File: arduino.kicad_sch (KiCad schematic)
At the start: 14 parts, among them J1 Conn_01x01_Female, J2 Conn_01x01_Female, J3 Conn_01x01_Female, J4 Conn_01x01_Female, J5 Conn_01x01_Female, J6 Conn_01x01_Female, J7 Conn_01x01_Female, U5 CD74HC4067SM, U6 LM358

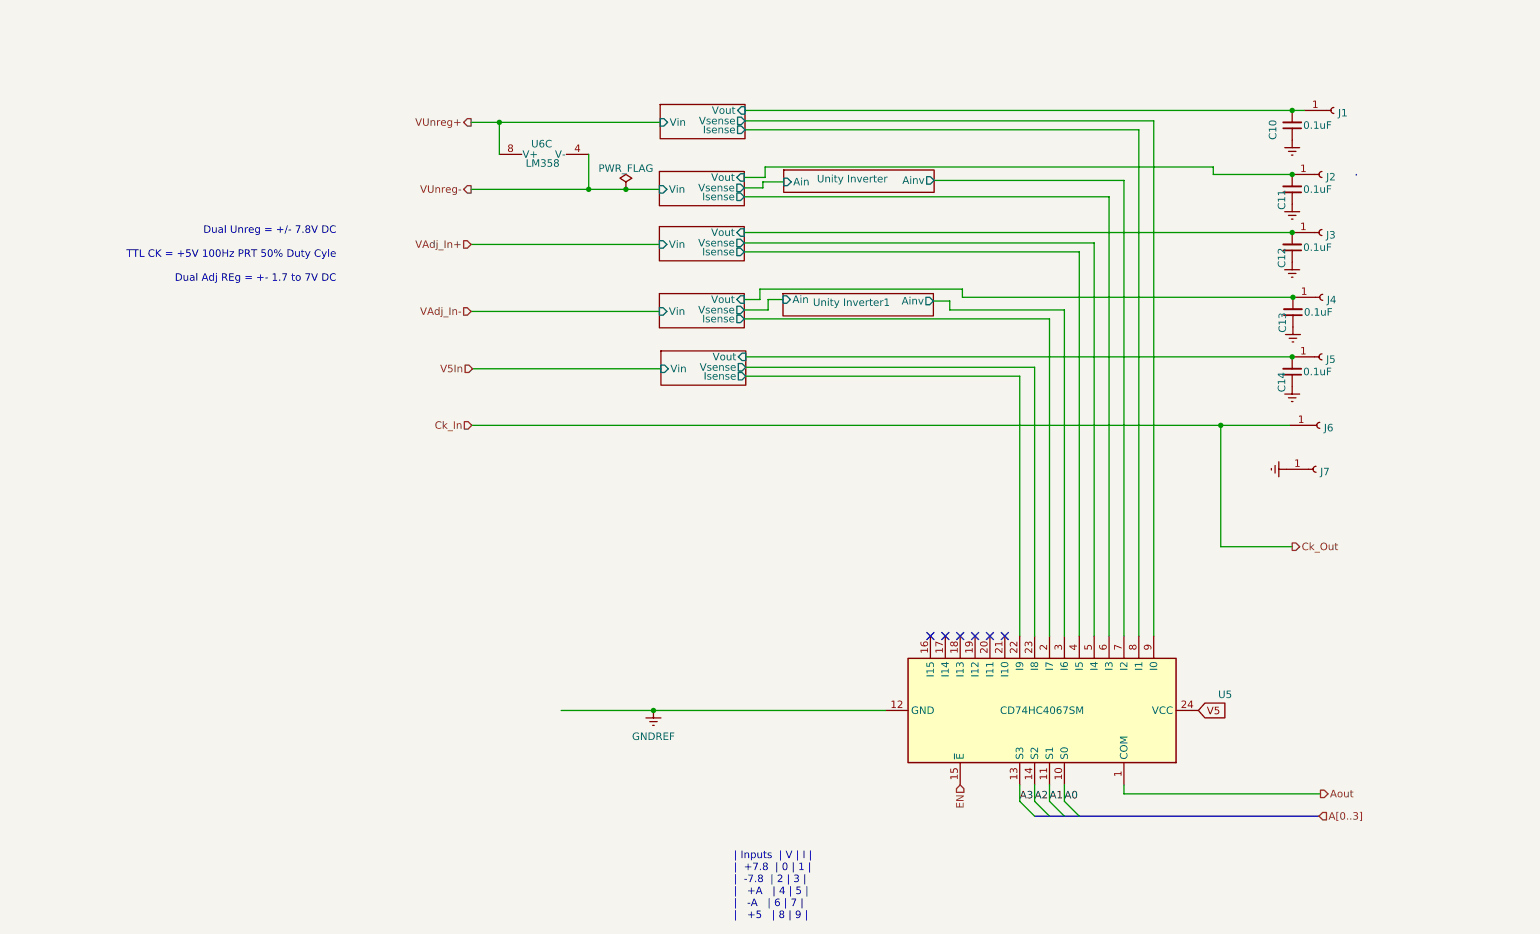
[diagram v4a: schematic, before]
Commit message: Updated improved board for all SMD
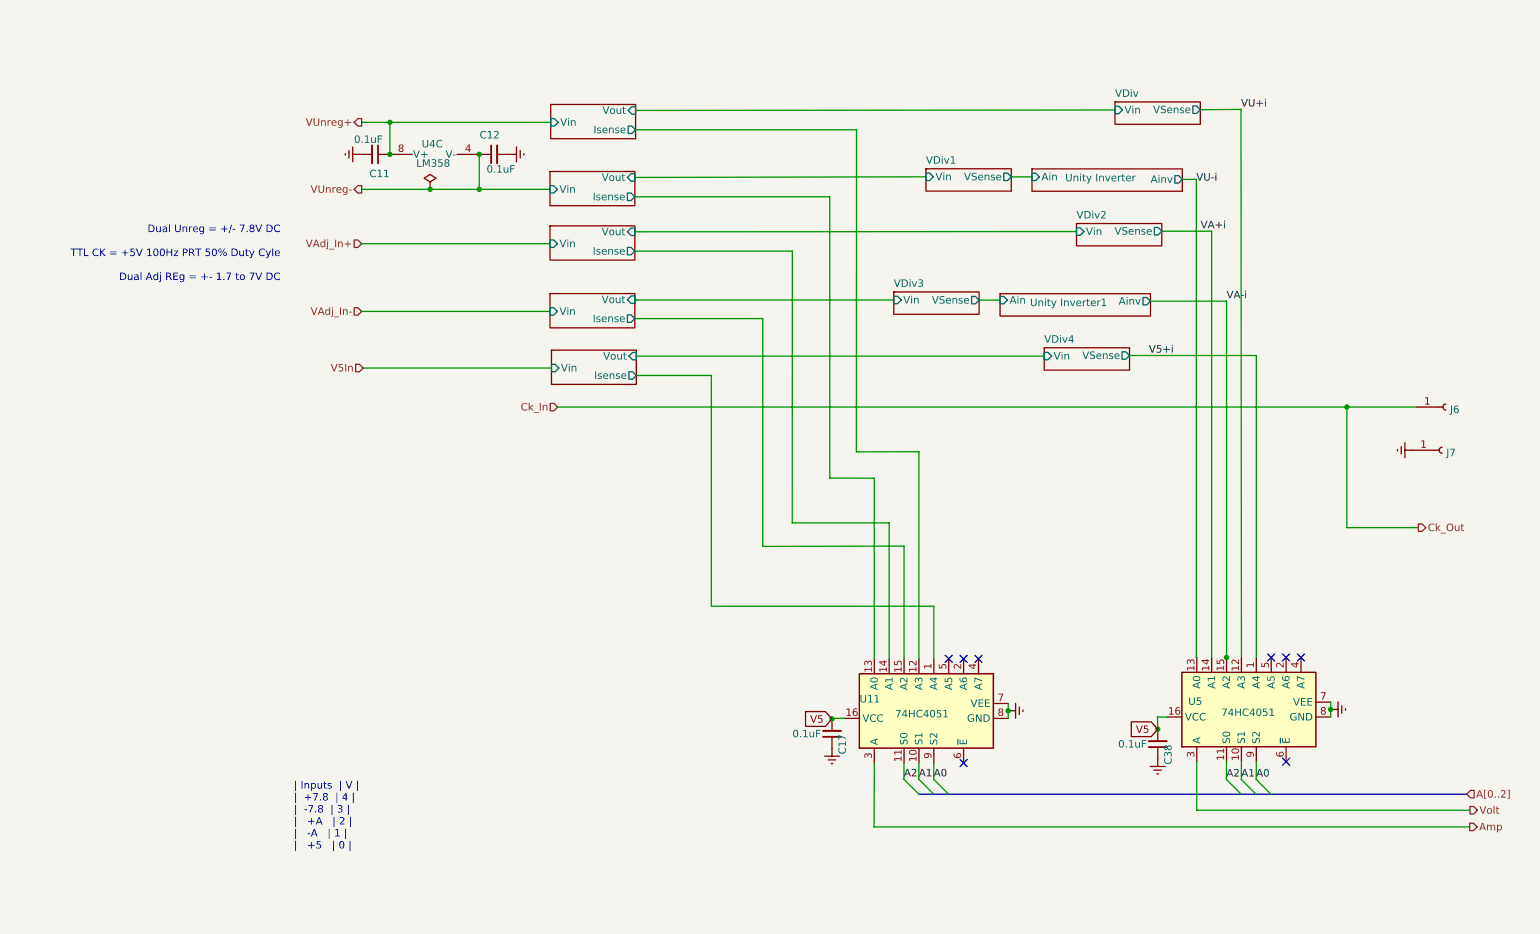
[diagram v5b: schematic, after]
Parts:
- removed C10, C13, C14: 0.1uF, Capacitor_SMD:C_0603_1608Metric, symbol Device:C_Small
- removed J1, J2, J3, J4, J5: Conn_01x01_Female, Connector_PinHeader_2.54mm:PinHeader_1x01_P2.54mm_Vertical, symbol Connector:Conn_01x01_Female
- removed U5: CD74HC4067SM, Package_SO:SSOP-24_5.3x8.2mm_P0.65mm, symbol 74xx:CD74HC4067SM
- added C17, C38: 0.1uF, Capacitor_SMD:C_0603_1608Metric, symbol Device:C_Small
- added U11, U5: 74HC4051, Package_SO:TSSOP-16-1EP_4.4x5mm_P0.65mm, symbol 74xx:74HC4051
- renumbered U6 to U4
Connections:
- net A0: now also U11.9 (S2), U5.9 (S2)
- net A1: now also U11.10 (S1), U5.10 (S1)
- net A2: now also U11.11 (S0), U5.11 (S0)
- net Curent and Volt4/Isense: now also U11.12 (A3)
- net Curent and Volt5/Isense: now also U11.13 (A0)
- net Curent and Volt5/Vout: no longer C11.2
- net Curent and Volt6/Isense: now also U11.14 (A1)
- net Curent and Volt6/Vout: no longer C12.2
- net Curent and Volt7/Isense: now also U11.15 (A2)
- net Curent and Volt8/Isense: now also U11.1 (A4)
- net GNDREF: now also C11.2, C12.2, C17.1, C38.1, U11.7 (VEE), U11.8 (GND), U5.7 (VEE), U5.8 (GND); no longer C11.1, C12.1
- net V5: now also C17.2, C38.2, U11.16 (VCC), U5.16 (VCC)
- net VUnreg+: now also C11.1
- net VUnreg-: now also C12.1
- new net Amp: U11.3 (A)
- new net V5+i: U5.1 (A4)
- new net VA+i: U5.14 (A1)
- new net VA-i: U5.15 (A2)
- new net VU+i: U5.12 (A3)
- new net VU-i: U5.13 (A0)
- new net Volt: U5.3 (A)
- no-connect marks 6 -> 8
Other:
- added sheet VDiv (VoltDivider.kicad_sch)
- added sheet VDiv1 (VoltDivider.kicad_sch)
- added sheet VDiv2 (VoltDivider.kicad_sch)
- added sheet VDiv3 (VoltDivider.kicad_sch)
- added sheet VDiv4 (VoltDivider.kicad_sch)
- sheet Curent and Volt4 ports: added none; removed Vsense
- sheet Curent and Volt5 ports: added none; removed Vsense
- sheet Curent and Volt6 ports: added none; removed Vsense
- sheet Curent and Volt7 ports: added none; removed Vsense
- sheet Curent and Volt8 ports: added none; removed Vsense
- note added: "| Inputs | V | | +7.8 | 4 | | -7.8 | 3 | | +A | 2 | | -A | 1 | | +5 | 0 |"
- note removed: "| Inputs | V | I | | +7.8 | 0 | 1 | | -7.8 | 2 | 3 | | +A | 4 | 5 | | -A | 6 | 7 | | +5 | 8 | 9 |"
- moved on the sheet: J6, J7, U4C

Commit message: added PDF schematic and images of board to date
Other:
- note removed: "| Inputs | V | | +7.8 | 4 | | -7.8 | 3 | | +A | 2 | | -A | 1 | | +5 | 0 |"
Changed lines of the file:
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@@
   (junction (at 89.789 41.656) (diameter 0) (color 0 0 0 0)
-  )
-  (junction (at 217.2716 127.4826) (diameter 0) (color 0 0 0 0)
   )
   (junction (at 237.7948 84.7598) (diameter 0) (color 0 0 0 0)
@@
     (stroke (width 0) (type default) (color 0 0 0 0))
   )
-  (wire (pts (xy 217.2716 127.7366) (xy 217.2716 127.4826))
-    (stroke (width 0) (type default) (color 0 0 0 0))
-  )
   (wire (pts (xy 149.5806 48.895) (xy 116.332 48.895))
     (stroke (width 0) (type default) (color 0 0 0 0))
@@
     (stroke (width 0) (type default) (color 0 0 0 0))
   )
-  (text "| Inputs  | V |\n|  +7.8  | 4 |\n|  -7.8  | 3 |\n|   +A   | 2 |\n|   -A   | 1 |\n|   +5   | 0 |"
-    (at 58.166 160.4772 0)
-    (effects (font (size 1.27 1.27)) (justify left bottom))
-  )
   (text "Dual Unreg = +/- 7.8V DC\n\nTTL CK = +5V 100Hz PRT 50% Duty Cyle\n\nDual Adj REg = +- 1.7 to 7V DC"

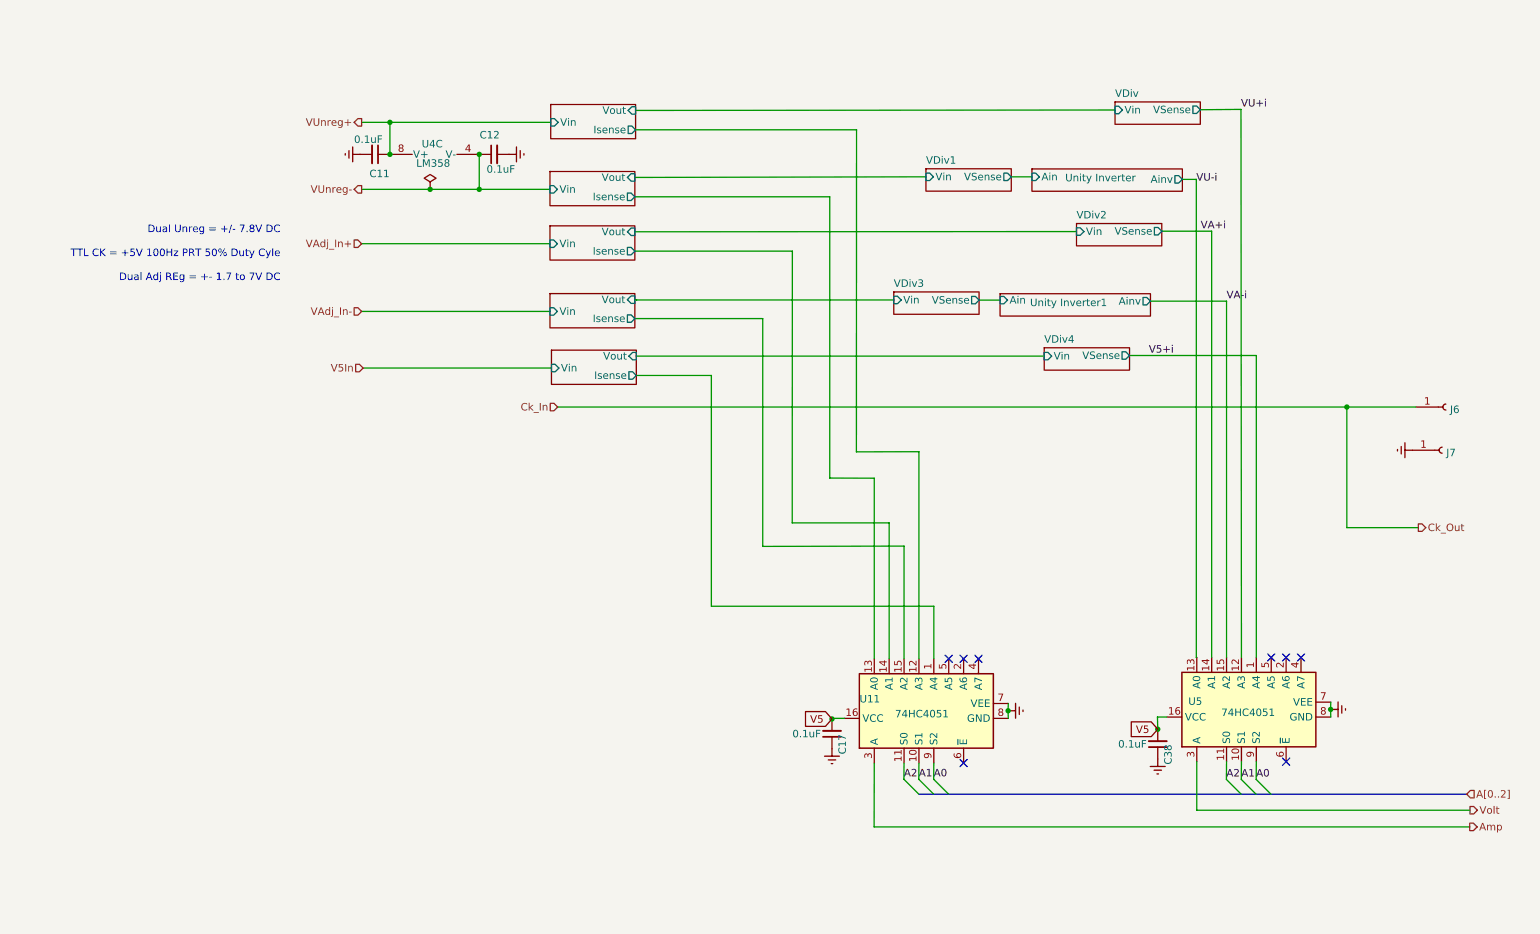
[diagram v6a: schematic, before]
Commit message: Refined board and kerned size down
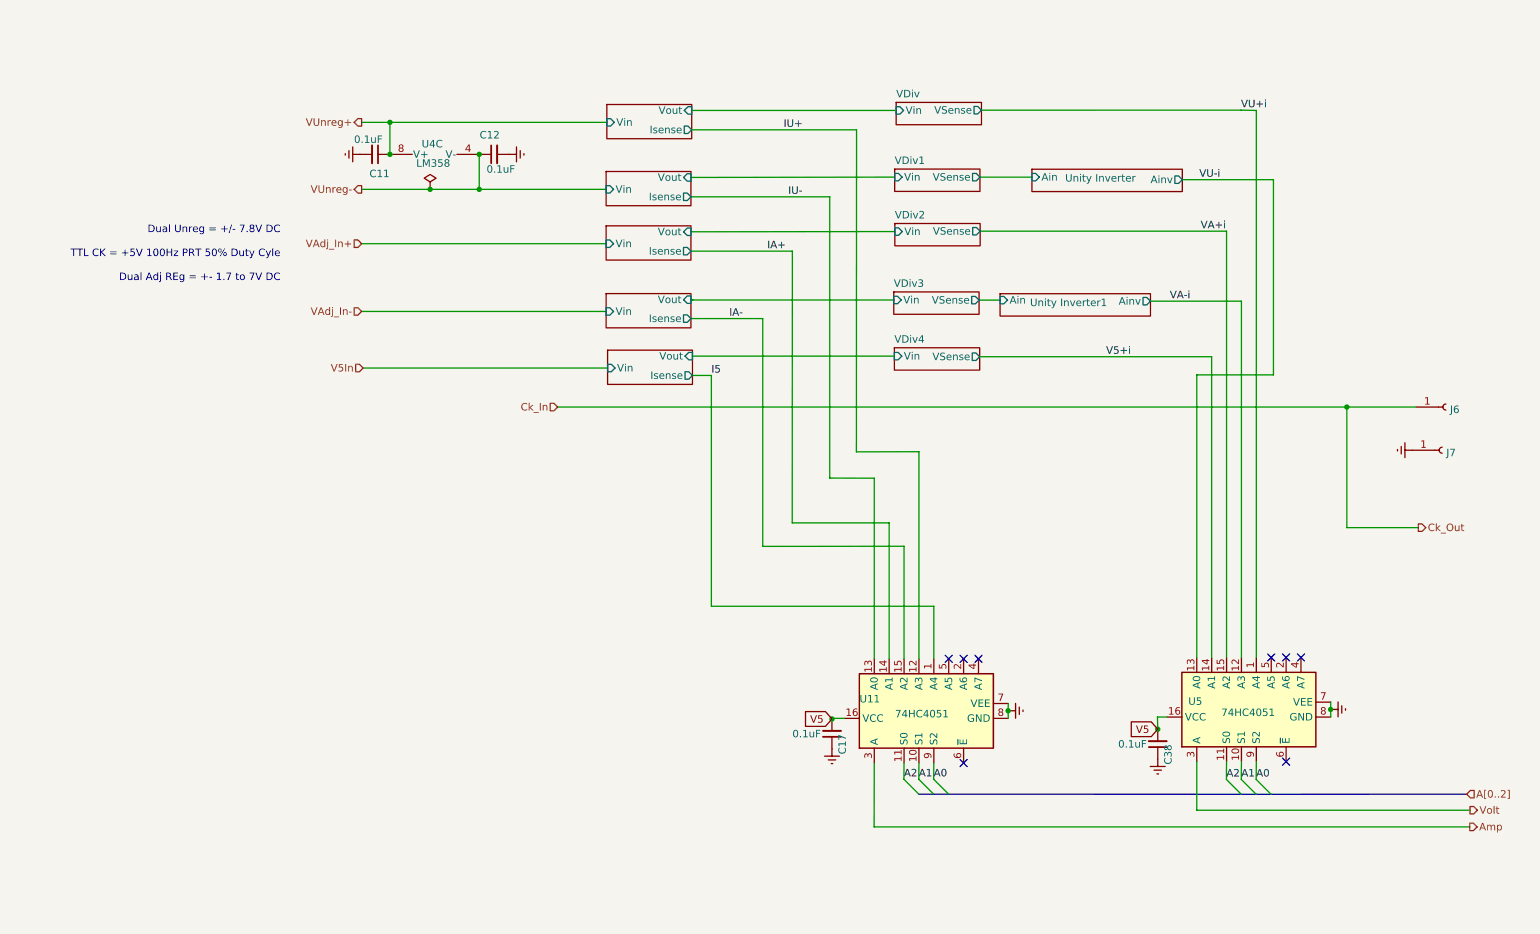
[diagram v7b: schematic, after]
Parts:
- U11, U5: footprint Package_SO:TSSOP-16-1EP_4.4x5mm_P0.65mm -> Package_SO:TSSOP-16_4.4x5mm_P0.65mm
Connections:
- net V5+i: now also U5.14 (A1); no longer U5.1 (A4)
- net VA+i: now also U5.15 (A2); no longer U5.14 (A1)
- net VA-i: now also U5.12 (A3); no longer U5.15 (A2)
- net VU+i: now also U5.1 (A4); no longer U5.12 (A3)
- net Curent and Volt4/Isense renamed IU+
- net Curent and Volt5/Isense renamed IU-
- net Curent and Volt6/Isense renamed IA+
- net Curent and Volt7/Isense renamed IA-
- net Curent and Volt8/Isense renamed I5

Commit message: further refining board size, adding rotary encoder and OLED display
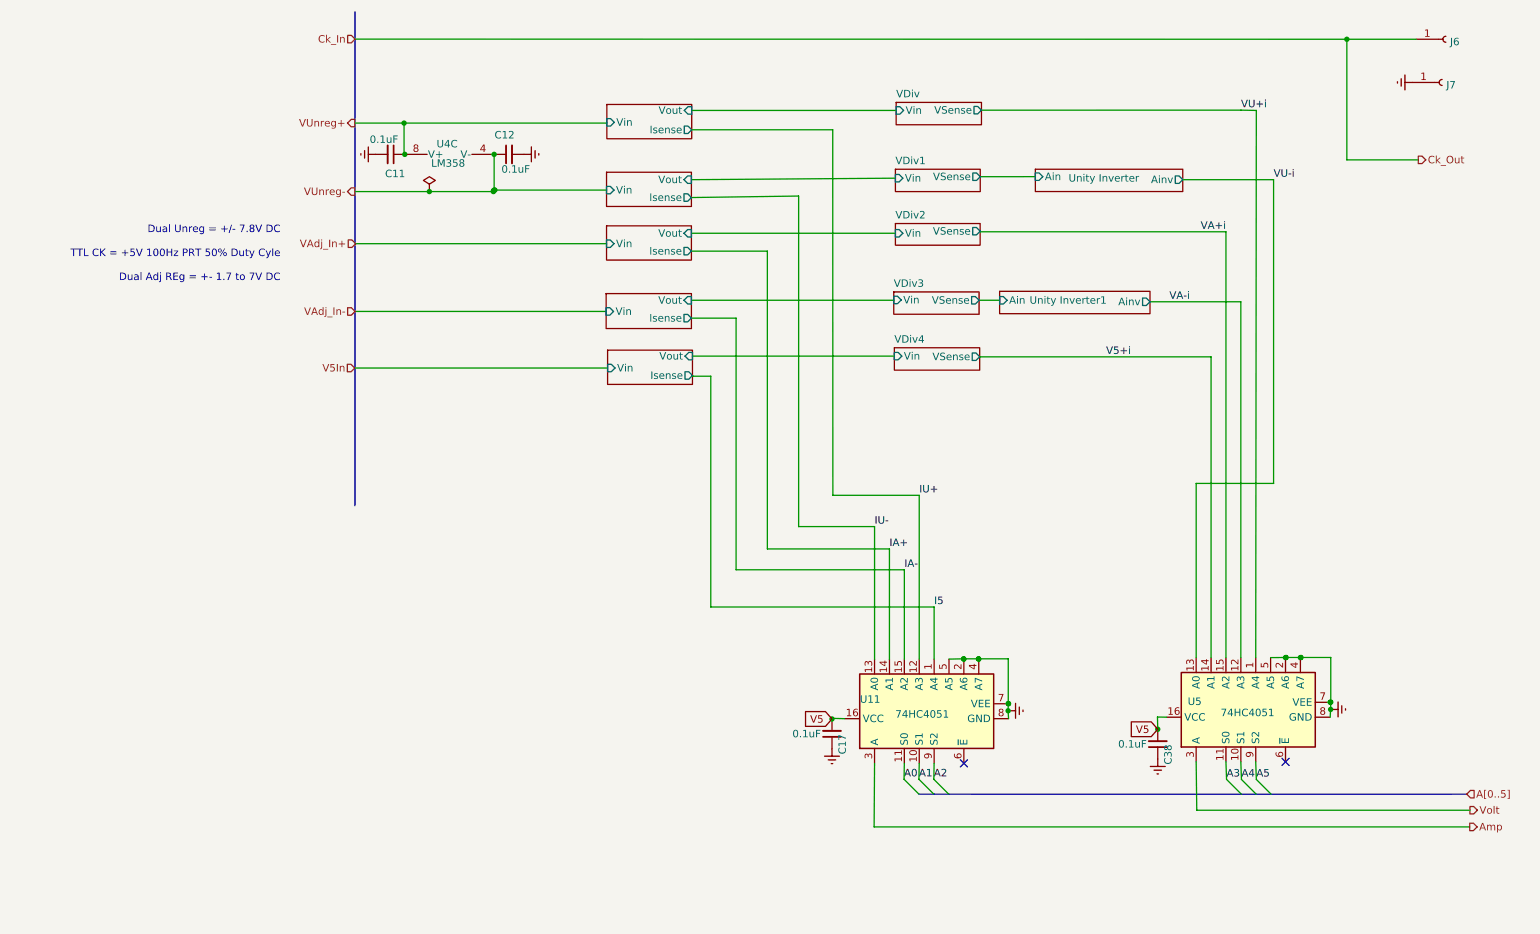
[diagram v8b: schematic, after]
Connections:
- net A0: now also U11.11 (S0); no longer U11.9 (S2), U5.9 (S2)
- net A1: no longer U5.10 (S1)
- net A2: now also U11.9 (S2); no longer U11.11 (S0), U5.11 (S0)
- net GNDREF: now also U11.2 (A6), U11.4 (A7), U11.5 (A5), U5.2 (A6), U5.4 (A7), U5.5 (A5)
- new net A3: U5.11 (S0)
- new net A4: U5.10 (S1)
- new net A5: U5.9 (S2)
- no-connect marks 8 -> 2
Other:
- moved on the sheet: C11, C12, J6, J7, U4C
